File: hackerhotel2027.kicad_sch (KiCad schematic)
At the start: 358 parts, among them J1 USB device, J2 Battery, Q1 JSM2301S, U1 CH643Q, U2 TPD4E05U06DQAR, U4 XT4054K421MR-G

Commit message: Add IR, add programming and UART headers, add buttons
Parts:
- added CGQ1: DY-IRMHF384-T05-2.5KB, infrared:OPTO-SMD_4P-L3.9-W3.4_IRM-H432M3-R8, symbol infrared:DY-IRMHF384-T05-2.5KB
- added D316: IR LED, LED_SMD:LED_0603_1608Metric, symbol Device:LED
- added J3: UART, Connector_PinHeader_2.54mm:PinHeader_1x04_P2.54mm_Vertical, symbol Connector_Generic:Conn_01x04
- added J4: Debug, Connector_PinHeader_2.54mm:PinHeader_1x04_P2.54mm_Vertical, symbol Connector_Generic:Conn_01x04
- added R25, R26, R27, R28, R34, R35: 10k, Resistor_SMD:R_0402_1005Metric, symbol symbols:R
- added R36, R37: 47, Resistor_SMD:R_0402_1005Metric, symbol Device:R
- added SW1, SW2, SW3, SW4: TS-1187A-B-A-B, pushbutton:SW-SMD_4P-L5.1-W5.1-P3.70-LS6.5-TL_H1.5, symbol pushbutton:TS-1187A-B-A-B
- C1: renamed from C54; LCSC C19702 -> (none); LCSC Part (none) -> C19702
- C2: renamed from C55; LCSC C1525 -> (none); LCSC Part (none) -> C1525
- C3: renamed from C56; LCSC C19702 -> (none); LCSC Part (none) -> C19702
- D1, D10, D100, D101, D102, D103, D104, D105, D106, D107, D108, D109, D11, D110, D111, D112, D113, D114, D115, D116, D117, D118, D119, D12, D120, D121, D122, D123, D124, D125, D126, D127, D128, D129, D13, D130, D131, D132, D133, D134, D135, D136, D137, D138, D139, D14, D140, D141, D142, D143, D144, D145, D146, D147, D148, D149, D15, D150, D158, D159, D16, D160, D161, D162, D163, D164, D165, D166, D167, D168, D169, D17, D170, D171, D172, D173, D174, D175, D176, D177, D178, D179, D18, D180, D181, D182, D183, D184, D185, D186, D187, D188, D189, D19, D190, D191, D192, D193, D194, D195, D196, D197, D198, D199, D2, D20, D200, D201, D202, D203, D204, D205, D206, D207, D208, D21, D216, D217, D218, D219, D22, D220, D221, D222, D223, D224, D225, D226, D227, D228, D229, D23, D230, D231, D232, D233, D234, D235, D236, D237, D238, D239, D24, D240, D241, D242, D243, D244, D245, D246, D247, D248, D249, D25, D250, D251, D252, D253, D254, D255, D256, D257, D258, D259, D26, D260, D261, D262, D263, D264, D265, D266, D27, D274, D275, D276, D277, D278, D279, D28, D280, D281, D282, D283, D284, D285, D286, D287, D288, D289, D29, D290, D291, D292, D293, D294, D295, D296, D297, D298, D299, D3, D30, D300, D301, D302, D303, D304, D305, D306, D307, D308, D309, D31, D310, D311, D312, D313, D314, D32, D33, D34, D4, D42, D43, D44, D45, D46, D47, D48, D49, D5, D50, D51, D52, D53, D54, D55, D56, D57, D58, D59, D6, D60, D61, D62, D63, D64, D65, D66, D67, D68, D69, D7, D70, D71, D72, D73, D74, D75, D76, D77, D78, D79, D8, D80, D81, D82, D83, D84, D85, D86, D87, D88, D89, D9, D90, D91, D92: LCSC Part C779450 -> C52675968
- D315: renamed from D316; LCSC C191023 -> (none); LCSC Part (none) -> C191023
- J2: LCSC Part (none) -> C20598817
- JP1: renamed from JP2; LCSC Part (none) -> -
- JP2: renamed from JP1; LCSC Part (none) -> -
- Q1: LCSC C916399 -> (none)
- R31: renamed from R28; LCSC C25744 -> (none); LCSC Part (none) -> C25744
- R32: renamed from R27; LCSC C4109 -> (none); LCSC Part (none) -> C4109
- R33: renamed from R29; LCSC C25741 -> (none); LCSC Part (none) -> C25741
- U3: renamed from U4; LCSC C141405 -> (none); LCSC Part (none) -> C141405
- renumbered C1 to C4, C2 to C5, C3 to C6, R25 to R29, R26 to R30
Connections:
- net T4 is gone; now on net VBUS: U1.12 (PC3/RTS2_/T1C4_)
- net GND: now also CGQ1.3 (GND), CGQ1.4 (GND), J3.4 (Pin_4), J4.4 (Pin_4), SW1.3 (C), SW2.3 (C), SW3.3 (C), SW4.3 (C)
- net SWCK: now also J4.2 (Pin_2)
- net SWIO: now also J4.1 (Pin_1)
- net VCC: now also J3.3 (Pin_3), J4.3 (Pin_3), R25.2, R26.2, R27.2, R28.2, R34.2
- net R19b: now reaches D152.2, D210.2, D268.2, D309.2 (A), D36.2, D94.2, R19.2
- net R18b: now reaches D151.2, D209.2, D267.2, D308.2 (A), D35.2, D93.2, R18.2
- net R23b: now reaches D156.2, D214.2, D272.2, D313.2 (A), D40.2, D98.2, R23.2
- net R17b: now reaches D116.2 (A), D133.2 (A), D150.2 (A), D17.2 (A), D174.2 (A), D191.2 (A), D208.2 (A), D232.2 (A), D249.2 (A), D266.2 (A), D290.2 (A), D307.2 (A), D34.2 (A), D58.2 (A), D75.2 (A), D92.2 (A), R17.2
- net R15b: now reaches D114.2 (A), D131.2 (A), D148.2 (A), D15.2 (A), D172.2 (A), D189.2 (A), D206.2 (A), D230.2 (A), D247.2 (A), D264.2 (A), D288.2 (A), D305.2 (A), D32.2 (A), D56.2 (A), D73.2 (A), D90.2 (A), R15.2
- net VBAT: now reaches C3.1, J2.1 (Pin_1), Q1.3 (D), U3.3 (V_{BAT})
- net R20b: now reaches D153.2, D211.2, D269.2, D310.2 (A), D37.2, D95.2, R20.2
- net R24b: now reaches D157.2, D215.2, D273.2, D314.2 (A), D41.2, D99.2, R24.2
- net R16b: now reaches D115.2 (A), D132.2 (A), D149.2 (A), D16.2 (A), D173.2 (A), D190.2 (A), D207.2 (A), D231.2 (A), D248.2 (A), D265.2 (A), D289.2 (A), D306.2 (A), D33.2 (A), D57.2 (A), D74.2 (A), D91.2 (A), R16.2
- net R21b: now reaches D154.2, D212.2, D270.2, D311.2 (A), D38.2, D96.2, R21.2
- net R22b: now reaches D155.2, D213.2, D271.2, D312.2 (A), D39.2, D97.2, R22.2
- net BTN2: now reaches U1.19 (PC4/CS_/T1BK_/T2ET_19)
- net BTN2: now also R26.1, SW2.2 (B)
- net BTN3: now reaches U1.20 (PC5/SCK_/T1C1N_20)
- net BTN3: now also R27.1, SW3.2 (B)
- net UART_TX: now reaches U1.36 (PB16/TX3_/T2C1_36)
- net UART_TX: now also J3.2 (Pin_2)
- net UART_RX: now reaches U1.37 (PB17/T2C2_/RX3_37)
- net UART_RX: now also J3.1 (Pin_1), R34.1
- net BTN4: now reaches U1.38 (PB18/T2C3_/CTS3_38)
- net BTN4: now also R28.1, SW4.2 (B)
- net IR_RECV: now reaches U1.39 (PB19/RTS3_/T2C4_39)
- net IR_RECV: now also CGQ1.1 (VOUT), R35.2
- net BTN1: now reaches U1.50 (PB20)
- net BTN1: now also R25.1, SW1.2 (B)
- net IR_LED-: now reaches U1.51 (PB21/T2C1_/CS_/RTS4_)
- net IR_LED-: now also D316.1 (K)
- net IR_LED+: now reaches U1.53 (PB23/T1C4_)
- net IR_LED+: now also R37.1
- net T1: no longer names the net of U1.9 (PC0/TX2_/T2C4_)
- net T2: no longer names the net of U1.10 (PC1/T1C2_/T2C1N_)
- net T3: no longer names the net of U1.11 (PC2/T1C3_/T2C2N_)
- new net: D316.2 (A), R37.2
- new net: CGQ1.2 (VCC), R36.2
- new net +3.3V: R35.1, R36.1
- no-connect marks 2 -> 11

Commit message: More routing
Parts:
- removed JP1: CC1, Jumper:SolderJumper-2_P1.3mm_Open_RoundedPad1.0x1.5mm, symbol Jumper:Jumper_2_Open
- removed JP2: CC2, Jumper:SolderJumper-2_P1.3mm_Open_RoundedPad1.0x1.5mm, symbol Jumper:Jumper_2_Open
- R37: value 47 -> 200; LCSC Part C22369545 -> (none)
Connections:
- net +3.3V is gone; now on net VCC: R35.1, R36.1
- net VCC: now also R37.1
- net CC1_ALT: no longer names the net of U1.55 (PC14/CC1/T1C3_/T2C2_)
- net CC2_ALT: no longer names the net of U1.56 (PC15/CC2/T2C3_/T1ET_)
- net IR_LED+: no longer names the net of U1.53 (PB23/T1C4_)
- net IR_LED+: no longer R37.1
- net IR_LED- renamed IR_LED

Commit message: More routing
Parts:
- removed J3: UART, Connector_PinHeader_2.54mm:PinHeader_1x04_P2.54mm_Vertical, symbol Connector_Generic:Conn_01x04
- removed J4: Debug, Connector_PinHeader_2.54mm:PinHeader_1x04_P2.54mm_Vertical, symbol Connector_Generic:Conn_01x04
- added J3: Debug, Connector_PinHeader_1.27mm:PinHeader_2x04_P1.27mm_Vertical, symbol Connector_Generic:Conn_02x04_Odd_Even
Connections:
- net BTN2: now also U1.20 (PC5/SCK_/T1C1N_20); no longer U1.19 (PC4/CS_/T1BK_/T2ET_19)
- net BTN3: now also U1.19 (PC4/CS_/T1BK_/T2ET_19); no longer U1.20 (PC5/SCK_/T1C1N_20)
- net GND: now also J3.7 (Pin_7)
- net SWCK: now also J3.3 (Pin_3)
- net SWIO: now also J3.1 (Pin_1)
- net UART_RX: now also J3.2 (Pin_2)
- net UART_TX: now also J3.4 (Pin_4)
- net VCC: now also J3.5 (Pin_5)
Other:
- moved on the sheet: R34

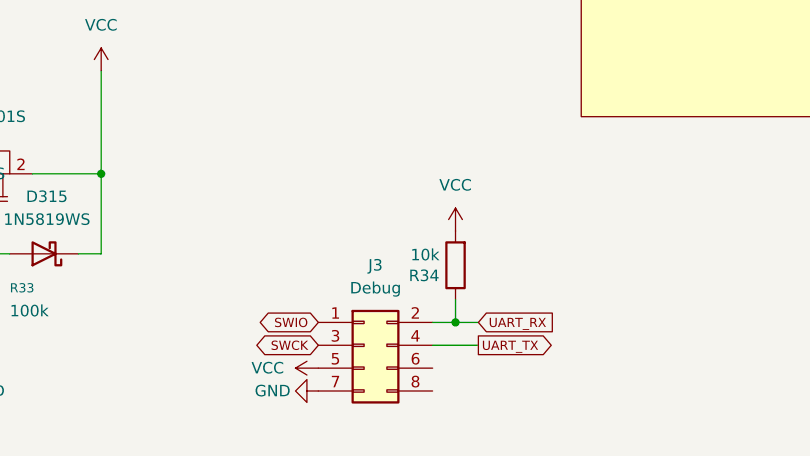
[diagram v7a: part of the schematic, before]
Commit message: Move IR, more routing, different debug connector
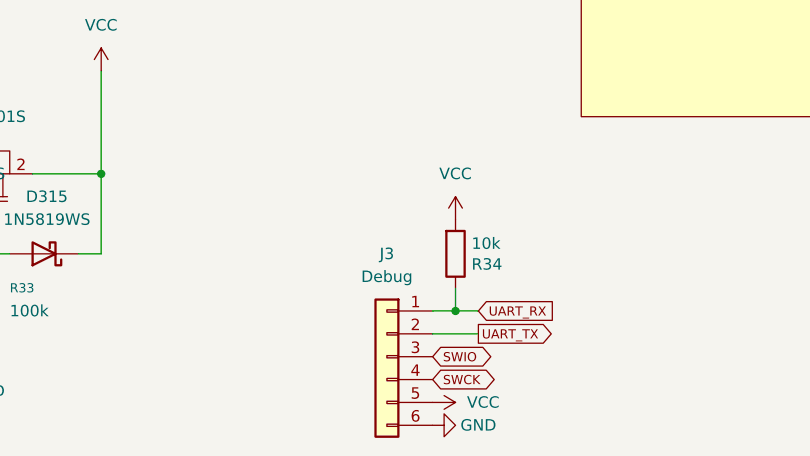
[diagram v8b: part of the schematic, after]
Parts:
- removed J3: Debug, Connector_PinHeader_1.27mm:PinHeader_2x04_P1.27mm_Vertical, symbol Connector_Generic:Conn_02x04_Odd_Even
- added J3: Debug, Connector_PinHeader_1.27mm:PinHeader_1x06_P1.27mm_Vertical, symbol Connector_Generic:Conn_01x06
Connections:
- net GND: now also J3.6 (Pin_6)
- net SWCK: now also J3.4 (Pin_4)
- net SWIO: now also J3.3 (Pin_3)
- net UART_RX: now also J3.1 (Pin_1)
- net UART_TX: now also J3.2 (Pin_2)
- net VCC: now also J3.5 (Pin_5)
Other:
- moved on the sheet: R34
